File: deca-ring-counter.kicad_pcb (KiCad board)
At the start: 2 copper layers, 165.3 x 128.5 mm, 93 parts, among them J1 PJ301M-12, J10 Conn_01x10_MountingPin, J11 Conn_01x10_MountingPin, J2 PJ301M-12, J3 PJ301M-12, J4 Conn_01x10_MountingPin, J5 Conn_01x04_MountingPin, J6 Conn_01x05_MountingPin, J7 Conn_01x04_MountingPin, J8 Conn_01x10_MountingPin, J9 Conn_01x05_MountingPin, Q1 BC547, Q2 BC547, SW1 SW_SPDT, SW10 SW_SPDT, SW2 SW_SPDT, SW3 SW_SPDT, SW4 SW_SPDT, SW5 SW_SPDT, SW6 SW_SPDT, SW7 SW_SPDT, SW8 SW_SPDT, SW9 SW_SPDT, U1 CD40106BPWR, U2 4017, U3 CD40106BPWR, U4 NE555P, U6 CD40106BPWR, U8 CD40106BPWR

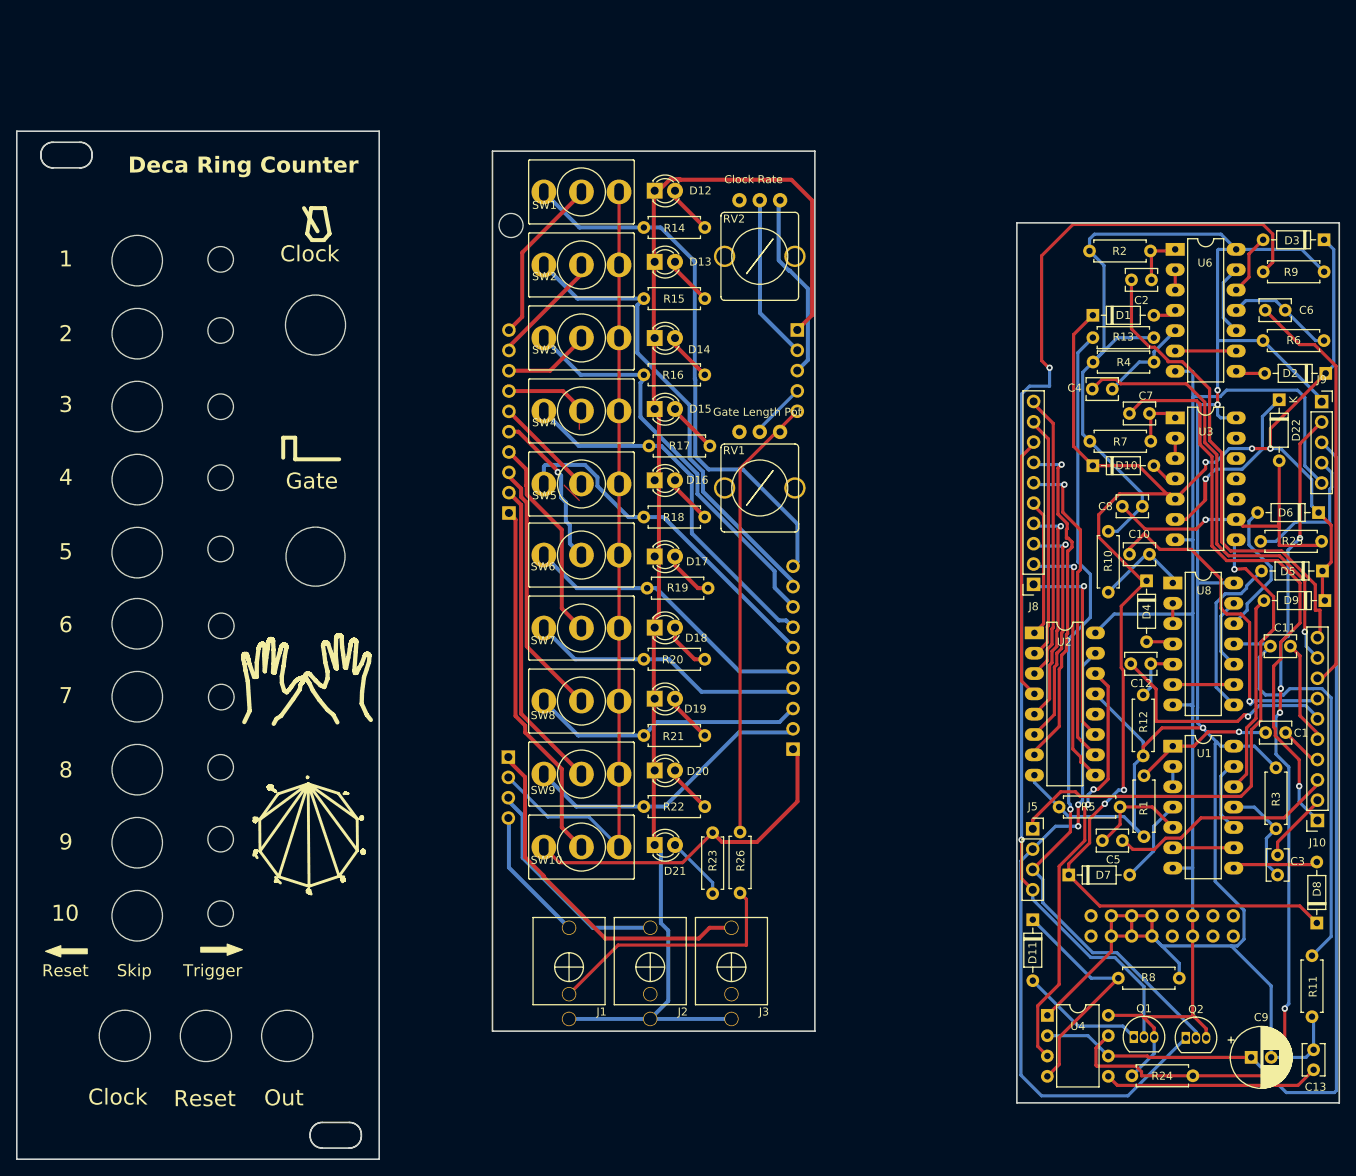
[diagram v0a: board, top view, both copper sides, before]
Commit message: Fixed critical routing bugs
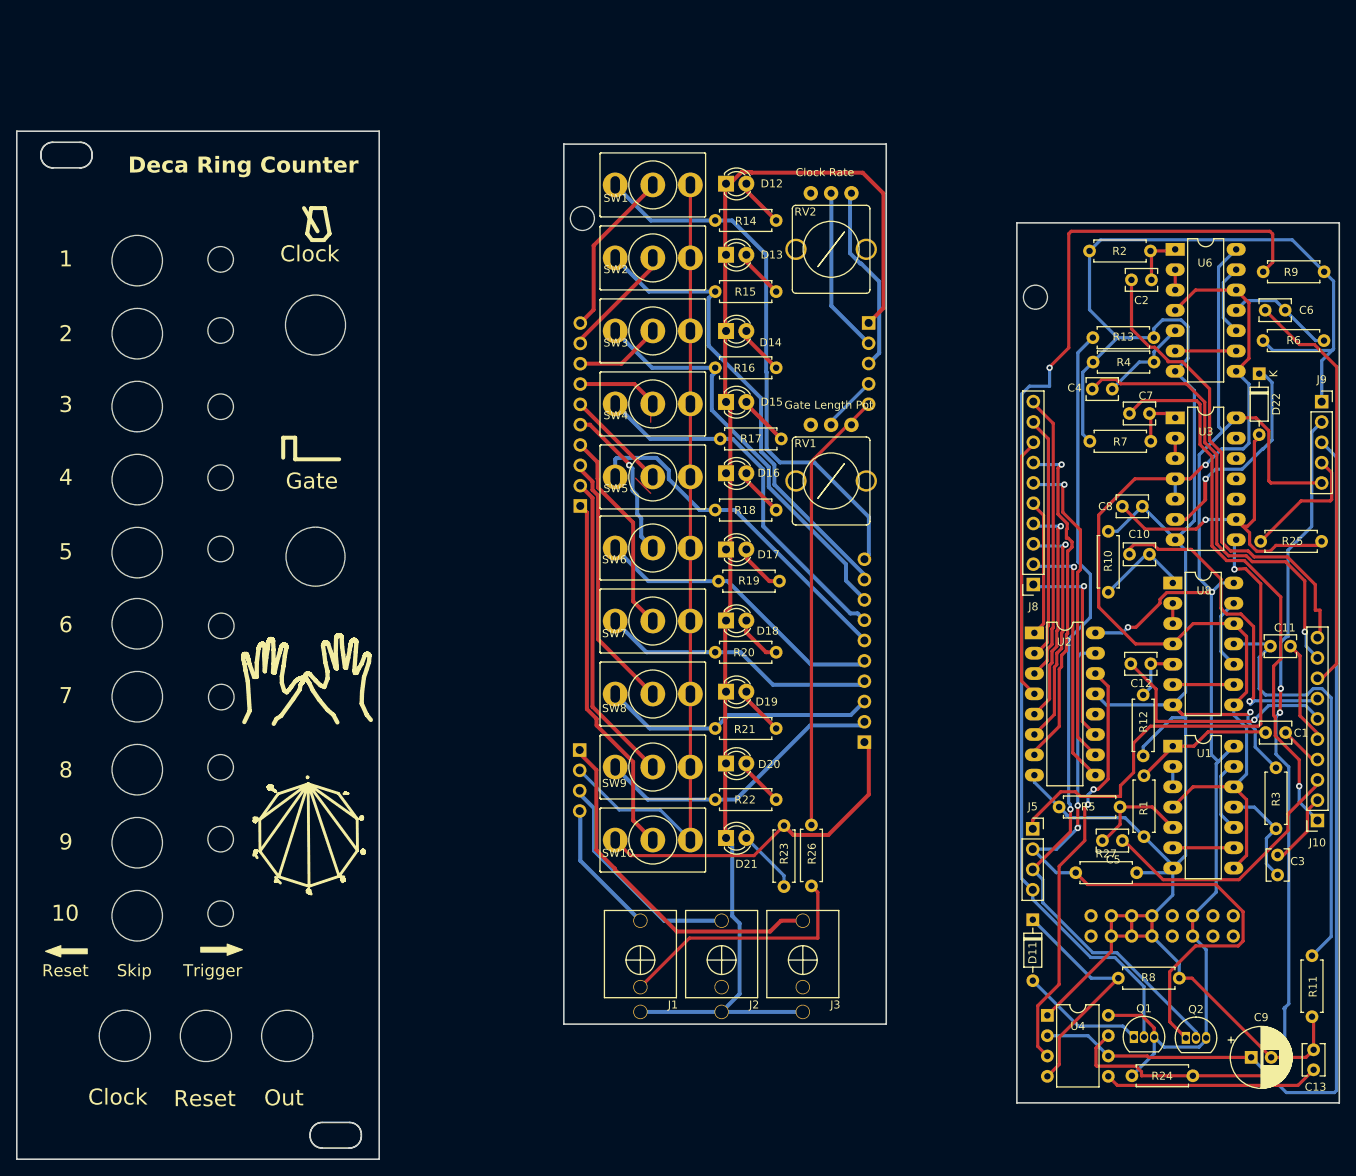
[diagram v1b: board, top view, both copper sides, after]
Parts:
- removed D1, D10, D2, D3, D4, D5, D6, D7, D8, D9: 1N4148, Diode_THT:D_DO-35_SOD27_P7.62mm_Horizontal
- added R27: 100k_0603, Resistor_THT:R_Axial_DIN0207_L6.3mm_D2.5mm_P7.62mm_Horizontal, F.Cu at (156.5, 122.2)
- moved J11 8.96 mm to (130.1, 105.9)
- moved J6 8.96 mm to (130.6, 53.5)
- moved J4 8.96 mm to (94.5, 76.3)
- moved R15 8.96 mm to (119.0, 49.5)
- moved D12 8.96 mm to (114.0, 36.0)
- moved D13 8.96 mm to (114.0, 44.9)
- moved D14 8.96 mm to (114.0, 54.5)
- moved D15 8.96 mm to (114.0, 63.3)
- moved D16 8.96 mm to (114.0, 72.2)
- moved D17 8.96 mm to (114.0, 81.8)
- moved D18 8.96 mm to (114.0, 90.7)
- moved D19 8.96 mm to (114.0, 99.5)
- moved D20 8.96 mm to (114.0, 108.5)
- moved D21 8.96 mm to (114.0, 117.8)
- moved J1 8.96 mm to (102.1, 133.1)
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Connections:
- U1 pad 12: Net-(D9-A) -> Net-(U1B-O)
- U1 pad 14: GND -> +5V
- U1 pad 4: Net-(D7-A) -> Net-(U1B-O)
- U1 pad 7: +5V -> GND
- U1 pad 8: Net-(D8-A) -> Net-(U1B-O)
- U3 pad 14: GND -> +5V
- U3 pad 4: Net-(D10-A) -> Net-(U1B-O)
- U3 pad 5: Net-(D1-K) -> Net-(U1B-O)
- U3 pad 7: +5V -> GND
- U6 pad 12: Net-(D3-A) -> Net-(U1B-O)
- U6 pad 14: GND -> +5V
- U6 pad 4: Net-(D1-A) -> Net-(U1B-O)
- U6 pad 7: +5V -> GND
- U6 pad 8: Net-(D2-A) -> Net-(U1B-O)
- U8 pad 12: Net-(D6-A) -> Net-(U1B-O)
- U8 pad 14: GND -> +5V
- U8 pad 4: Net-(D4-A) -> Net-(U1B-O)
- U8 pad 7: +5V -> GND
- U8 pad 8: Net-(D5-A) -> Net-(U1B-O)
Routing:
- net Net-(D1-K): track 198.2 -> 0.00 mm, vias 5 -> 0
- net Net-(U1B-O): track 0.00 -> 129.6 mm, vias 0 -> 1
- net Net-(D9-A): track 24.8 -> 0.00 mm
- net Net-(D5-A): track 21.1 -> 0.00 mm
- net GND: track 335.7 -> 316.2 mm, vias 3 -> 1
- net Net-(D6-A): track 17.4 -> 0.00 mm
- net +5V: track 152.8 -> 168.2 mm, vias 0 -> 2
- net Net-(D8-A): track 11.8 -> 0.00 mm
- net Net-(D7-A): track 10.7 -> 0.00 mm
- net Net-(D3-A): track 7.68 -> 0.00 mm
- net Net-(D22-A): track 38.3 -> 43.7 mm
- net /Circuit panel/trigger step 10: track 74.8 -> 70.3 mm
- net /Circuit panel/trigger step 8: track 28.4 -> 32.8 mm
- net Net-(D2-A): track 3.68 -> 0.00 mm
- net Net-(D22-K): track 25.8 -> 29.4 mm
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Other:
- outline, holes or cut-outs redrawn

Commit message: Version 1.3 of the model.
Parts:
- added D1: LED, eurocad:LED3mm, F.Cu at (125.5, 55.4)
- added Q3: BC547, Package_TO_SOT_THT:TO-92_Inline, F.Cu at (181.1, 73.7)
- added R28: 10k_0603, Resistor_THT:R_Axial_DIN0207_L6.3mm_D2.5mm_P7.62mm_Horizontal, F.Cu at (183.6, 66.0)
- added R29: 1k_0603, Resistor_THT:R_Axial_DIN0207_L6.3mm_D2.5mm_P7.62mm_Horizontal, F.Cu at (120.1, 62.0)
- added R30: 100k_0603, Resistor_THT:R_Axial_DIN0207_L6.3mm_D2.5mm_P7.62mm_Horizontal, F.Cu at (187.2, 84.6)
- RV1: value Gate Length Pot -> Gate Length
- moved R25 7.88 mm to (179.3, 80.5), turned to 0 degrees
- moved R9 2.36 mm to (180.1, 44.7)
- moved D22 0.70 mm to (180.1, 59.9)
- moved R16 0.13 mm to (119.0, 58.9)
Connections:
- U3 pad 10: (no net) -> Net-(U3E-O)
- U3 pad 11: (no net) -> Net-(U3E-I)
- U3 pad 12: (no net) -> Net-(U1B-O)
- U3 pad 13: (no net) -> Net-(U3E-O)
- U3 pad 8: /Circuit panel/gate_out -> Net-(Q3-B)
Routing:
- net /Front Panel/Gate out: track 43.5 -> 112.4 mm, vias 0 -> 1
- net Net-(U3E-I): track 0.00 -> 19.2 mm, vias 0 -> 2
- net /Circuit panel/gate_out: track 63.5 -> 80.3 mm
- net GND: track 316.2 -> 329.0 mm, vias 1 -> 2
- net Net-(D22-A): track 43.7 -> 32.9 mm
- net Net-(U3E-O): track 0.00 -> 8.95 mm
- net Net-(Q3-B): track 0.00 -> 8.25 mm
- net /Front Panel/Ground: track 163.4 -> 170.6 mm
- net Net-(D1-A): track 0.00 -> 7.02 mm
- net /Circuit panel/gate length: track 16.2 -> 11.5 mm
- net /Circuit panel/clock rate 1: track 115.2 -> 118.4 mm
- net /Circuit panel/clock in: track 143.6 -> 141.2 mm
- net Net-(D22-K): track 29.4 -> 31.1 mm
- net +5V: track 168.2 -> 169.7 mm
- net Net-(U1B-O): track 129.6 -> 130.9 mm
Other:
- board size 165.3 x 128.5 mm -> 157.7 x 135.8 mm
- board text added: "DRC v1.2"
- board text removed: "DRC v1.1"
